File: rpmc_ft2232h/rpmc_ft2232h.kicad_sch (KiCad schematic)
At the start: 4 parts, among them J1 Conn_02x20_Odd_Even, U2 74HC373, U3 74LS139

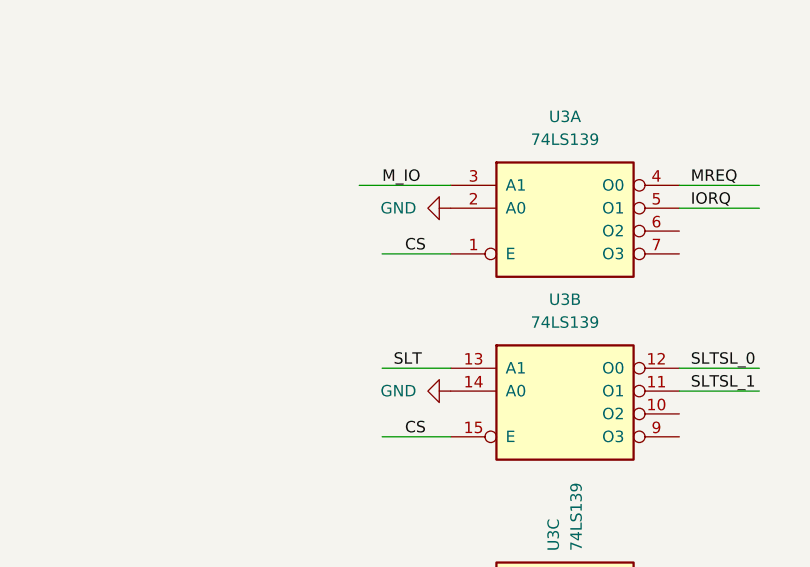
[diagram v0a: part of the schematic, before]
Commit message: rpmc_ft2232h/rpmc_ft2232h.kicad_pcb rpmc_ft2232h/rpmc_ft2232h.kicad_sch
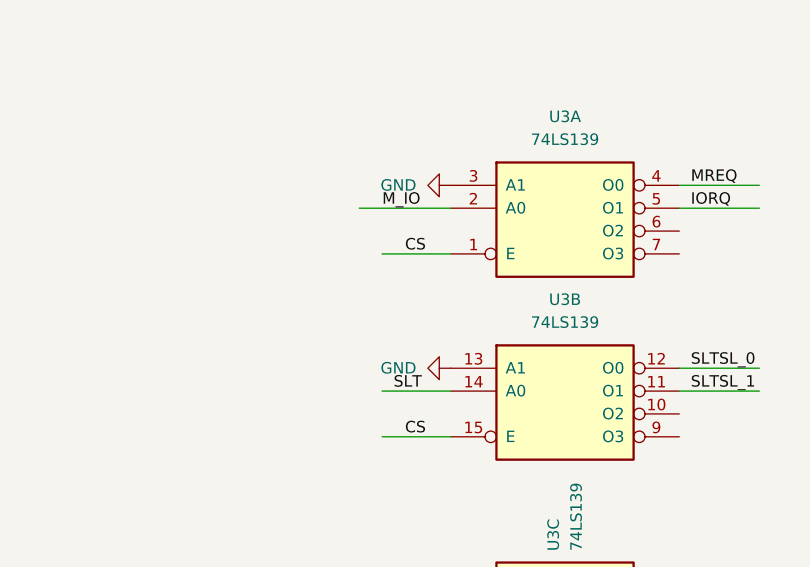
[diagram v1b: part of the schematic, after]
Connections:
- net GND: now also U3.13 (A1), U3.3 (A1); no longer U3.14 (A0), U3.2 (A0)
- net M_IO: now also U3.2 (A0); no longer U3.3 (A1)
- net SLT: now also U3.14 (A0); no longer U3.13 (A1)
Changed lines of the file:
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@@
 	(wire
 		(pts
-			(xy 49.53 152.4) (xy 57.15 152.4)
+			(xy 49.53 154.94) (xy 57.15 154.94)
 		)
 		(stroke
@@
 	(wire
 		(pts
-			(xy 46.99 132.08) (xy 57.15 132.08)
+			(xy 46.99 134.62) (xy 57.15 134.62)
 		)
 		(stroke
@@
 	)
 	(label "M_IO"
-		(at 49.53 132.08 0)
+		(at 49.53 134.62 0)
 		(fields_autoplaced yes)
 		(effects
@@
 	)
 	(label "SLT"
-		(at 50.8 152.4 0)
+		(at 50.8 154.94 0)
 		(fields_autoplaced yes)
 		(effects
@@
 	(symbol
 		(lib_id "power:GND")
-		(at 57.15 134.62 270)
+		(at 57.15 132.08 270)
+		(mirror x)
 		(unit 1)
 		(exclude_from_sim no)
@@
 		(fields_autoplaced yes)
 		(property "Reference" "#PWR08"
-			(at 50.8 134.62 0)
+			(at 50.8 132.08 0)
 			(effects
 				(font
@@
 		)
 		(property "Value" "GND"
-			(at 53.34 134.6199 90)
+			(at 53.34 132.0801 90)
 			(effects
 				(font
@@
 		)
 		(property "Footprint" ""
-			(at 57.15 134.62 0)
+			(at 57.15 132.08 0)
 			(effects
 				(font
@@
 		)
 		(property "Datasheet" ""
-			(at 57.15 134.62 0)
+			(at 57.15 132.08 0)
 			(effects
 				(font
@@
 		)
 		(property "Description" "Power symbol creates a global label with name \"GND\" , ground"
-			(at 57.15 134.62 0)
+			(at 57.15 132.08 0)
 			(effects
 				(font
@@
 	(symbol
 		(lib_id "power:GND")
-		(at 57.15 154.94 270)
+		(at 57.15 152.4 270)
+		(mirror x)
 		(unit 1)
 		(exclude_from_sim no)
@@
 		(fields_autoplaced yes)
 		(property "Reference" "#PWR09"
-			(at 50.8 154.94 0)
+			(at 50.8 152.4 0)
 			(effects
 				(font
@@
 		)
 		(property "Value" "GND"
-			(at 53.34 154.9399 90)
+			(at 53.34 152.4001 90)
 			(effects
 				(font
@@
 		)
 		(property "Footprint" ""
-			(at 57.15 154.94 0)
+			(at 57.15 152.4 0)
 			(effects
 				(font
@@
 		)
 		(property "Datasheet" ""
-			(at 57.15 154.94 0)
+			(at 57.15 152.4 0)
 			(effects
 				(font
@@
 		)
 		(property "Description" "Power symbol creates a global label with name \"GND\" , ground"
-			(at 57.15 154.94 0)
-			(effects
-				(font
+			(at 57.15 152.4 0)
+			(effects
+				(font
